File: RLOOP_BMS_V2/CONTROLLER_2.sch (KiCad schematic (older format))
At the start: 38 parts, among them U2 bq76PL536A_HTQFP

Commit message: More WIP
Added connector for 1-Wire sensors if we want to put some sensors on the
heat-sinks. Just need to double check everything with the 3d-models.
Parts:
- U2: symbol bq76PL536A_HTQFP -> bq76PL536A_HTQFP-RESCUE-rLoop_BMS_v2
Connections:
- wire segments 148 -> 149

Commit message: more WIP
So close. Need to finish arranging the sild screen and make sure diodes
get put on in the correct orientation.
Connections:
- net GND_2: now also U2.THRM
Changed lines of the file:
@@
 	6500 4200 6800 4200
 Wire Wire Line
-	6800 4200 6800 4850
+	6800 4100 6800 4850
 Wire Wire Line
 	6500 4300 6800 4300
@@
 Wire Wire Line
 	4250 3400 4100 3400
+Wire Wire Line
+	6500 4100 6800 4100
+Connection ~ 6800 4200
 $EndSCHEMATC

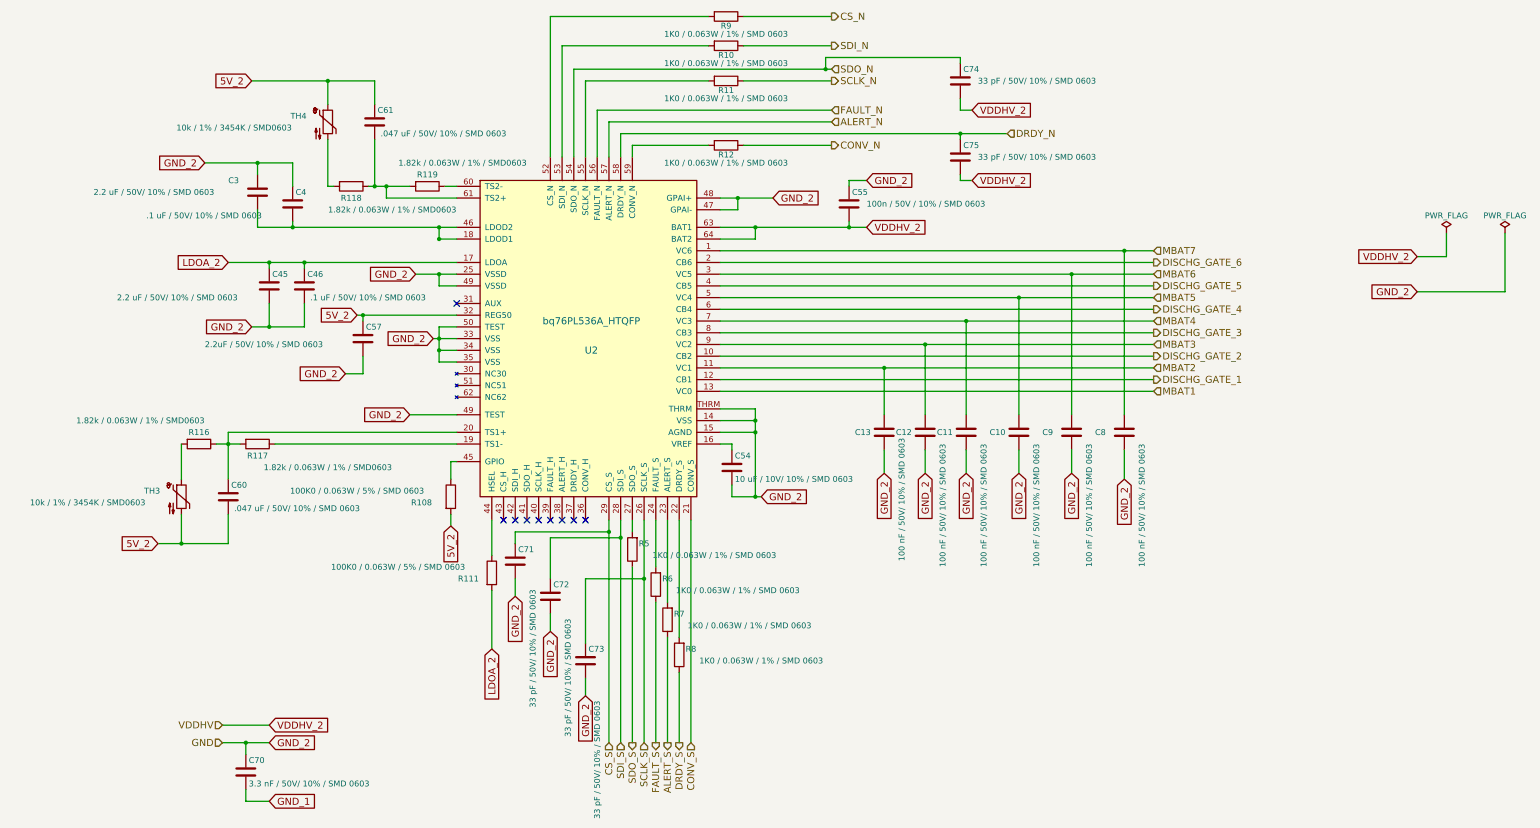
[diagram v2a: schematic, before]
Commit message: Updated page sizes for schematics
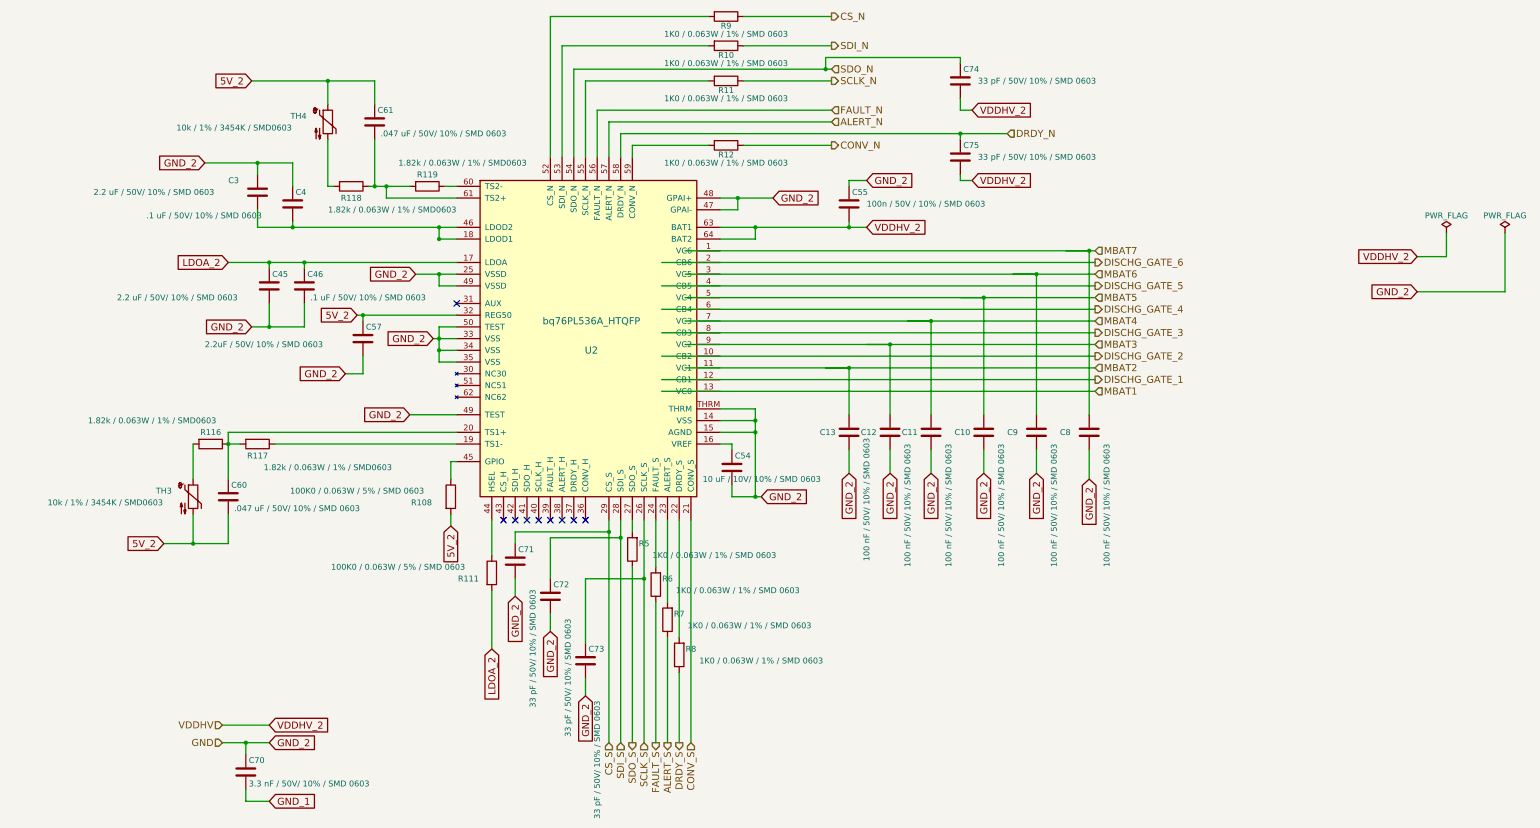
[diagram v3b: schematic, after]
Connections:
- wire segments 150 -> 185
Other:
- moved on the sheet: C10, C11, C12, C13, C8, C9, R116, TH3

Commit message: swapped a few connectors to standardize with the power node and what's readily available
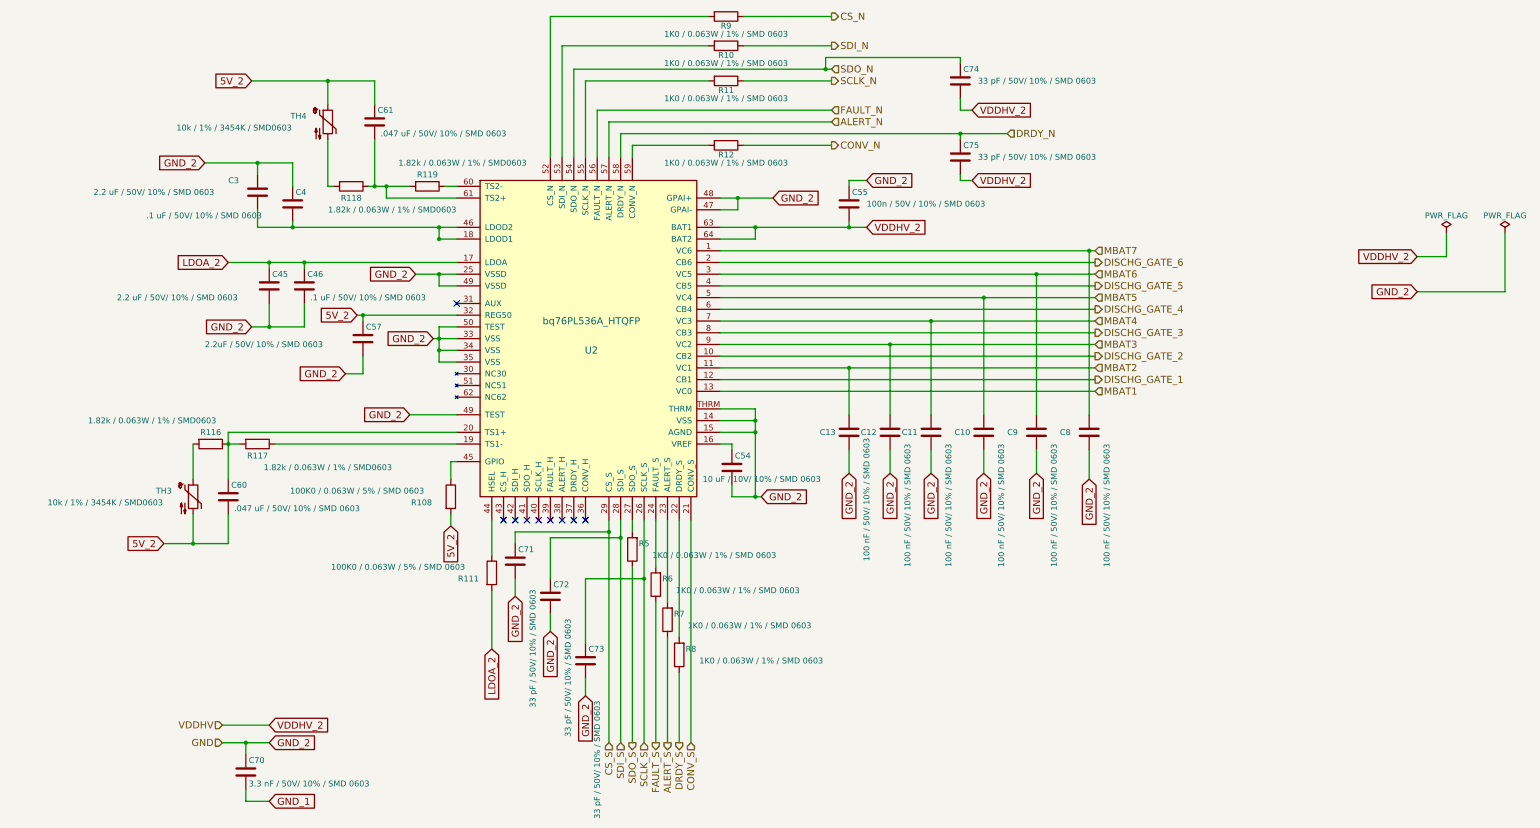
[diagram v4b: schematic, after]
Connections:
- wire segments 185 -> 150
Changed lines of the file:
@@
 	2250 6800 2650 6800
 Wire Wire Line
-	2250 6950 2450 6950
-Wire Wire Line
-	2450 6950 2650 6950
-Wire Wire Line
-	6200 2750 9650 2750
-Wire Wire Line
-	9450 2750 9700 2750
-Wire Wire Line
-	9700 2850 6000 2850
-Wire Wire Line
-	6200 2950 9200 2950
-Wire Wire Line
-	9000 2950 9700 2950
-Wire Wire Line
-	9700 3050 6000 3050
-Wire Wire Line
-	6200 3150 8750 3150
-Wire Wire Line
-	8550 3150 9700 3150
-Wire Wire Line
-	6000 3250 9700 3250
-Wire Wire Line
-	6200 3350 8300 3350
-Wire Wire Line
-	8100 3350 9700 3350
-Wire Wire Line
-	6000 3450 9700 3450
-Wire Wire Line
-	6200 3550 7950 3550
-Wire Wire Line
-	7750 3550 9700 3550
-Wire Wire Line
-	6000 3650 9700 3650
-Wire Wire Line
-	6200 3750 7600 3750
-Wire Wire Line
-	7400 3750 9700 3750
-Wire Wire Line
-	6000 3850 9700 3850
-Wire Wire Line
-	9700 3950 6000 3950
-Wire Wire Line
-	9650 4150 9650 2750
+	2250 6950 2650 6950
+Wire Wire Line
+	6500 2750 9700 2750
+Wire Wire Line
+	6500 2950 9700 2950
+Wire Wire Line
+	6500 3150 9700 3150
+Wire Wire Line
+	6500 3350 9700 3350
+Wire Wire Line
+	6500 3550 9700 3550
+Wire Wire Line
+	6500 3750 9700 3750
+Wire Wire Line
+	9650 2750 9650 4150
 Connection ~ 9650 2750
 Wire Wire Line
-	9200 4150 9200 2950
+	9200 2950 9200 4150
 Connection ~ 9200 2950
 Wire Wire Line
-	8750 4150 8750 3150
+	8750 3150 8750 4150
 Connection ~ 8750 3150
 Wire Wire Line
-	8300 4150 8300 3350
+	8300 3350 8300 4150
 Connection ~ 8300 3350
 Wire Wire Line
-	7950 4150 7950 3550
+	7950 3550 7950 4150
 Connection ~ 7950 3550
 Wire Wire Line
-	7600 4150 7600 3750
+	7600 3750 7600 4150
 Connection ~ 7600 3750
 Wire Wire Line
@@
 	7950 4650 7950 4450
 Wire Wire Line
-	3400 3300 3450 3300
-Wire Wire Line
-	3450 3300 4250 3300
-Wire Wire Line
-	4050 3500 4100 3500
-Wire Wire Line
-	4100 3500 4250 3500
-Wire Wire Line
-	4250 3600 4100 3600
-Wire Wire Line
-	4100 3400 4100 3500
-Wire Wire Line
-	4100 3500 4100 3600
-Wire Wire Line
-	4100 3600 4100 3700
+	3400 3300 4250 3300
+Wire Wire Line
+	4050 3500 4250 3500
+Wire Wire Line
+	4100 3600 4250 3600
+Wire Wire Line
+	4100 3400 4100 3700
 Connection ~ 4100 3500
 Wire Wire Line
@@
 	6500 4200 6800 4200
 Wire Wire Line
-	6800 4100 6800 4200
-Wire Wire Line
-	6800 4200 6800 4300
-Wire Wire Line
-	6800 4300 6800 4850
+	6800 4100 6800 4850
 Wire Wire Line
 	6500 4300 6800 4300
 Connection ~ 6800 4300
 Wire Wire Line
-	3900 2950 4100 2950
-Wire Wire Line
-	4100 2950 4250 2950
+	3900 2950 4250 2950
 Wire Wire Line
 	4250 3050 4100 3050
@@
 Connection ~ 4100 2950
 Wire Wire Line
-	6500 2550 6800 2550
-Wire Wire Line
-	6800 2550 7600 2550
-Wire Wire Line
-	7600 2550 7750 2550
+	6500 2550 7750 2550
 Wire Wire Line
 	6500 2650 6800 2650
@@
 	5250 1950 5250 1200
 Wire Wire Line
-	5250 1200 7400 1200
-Wire Wire Line
-	7400 1200 7450 1200
+	5250 1200 7450 1200
 Wire Wire Line
 	5350 1300 5350 1950
@@
 	5650 1950 5650 1750
 Wire Wire Line
-	5650 1750 8550 1750
-Wire Wire Line
-	8550 1750 8950 1750
+	5650 1750 8950 1750
 Wire Wire Line
 	5550 1950 5550 1650
@@
 	7450 1850 6700 1850
 Wire Wire Line
-	5550 5050 5550 5150
-Wire Wire Line
-	5550 5150 5550 6950
-Wire Wire Line
-	5650 5050 5650 5200
-Wire Wire Line
-	5650 5200 5650 6950
+	5550 5050 5550 6950
+Wire Wire Line
+	5650 5050 5650 6950
 Wire Wire Line
 	5750 5050 5750 5150
@@
 	5750 5450 5750 6950
 Wire Wire Line
-	5850 5050 5850 5550
-Wire Wire Line
-	5850 5550 5850 6950
+	5850 5050 5850 6950
 Wire Wire Line
 	5950 5050 5950 5450
@@
 	5950 5750 5950 6950
 Wire Wire Line
-	2100 2000 2550 2000
-Wire Wire Line
-	2550 2000 2850 2000
+	2100 2000 2850 2000
 Wire Wire Line
 	2550 2000 2550 2100
@@
 Connection ~ 2850 2550
 Wire Wire Line
-	2550 2550 2850 2550
-Wire Wire Line
-	2850 2550 4100 2550
-Wire Wire Line
-	4100 2550 4250 2550
+	2550 2550 4250 2550
 Wire Wire Line
 	2550 2550 2550 2400
@@
 	4100 2650 4250 2650
 Wire Wire Line
-	2500 3400 2650 3400
-Wire Wire Line
-	2650 3400 2950 3400
+	2500 3400 2950 3400
 Wire Wire Line
 	2950 3400 2950 3200
@@
 	2650 2900 2650 2850
 Wire Wire Line
-	2300 2850 2650 2850
-Wire Wire Line
-	2650 2850 2950 2850
-Wire Wire Line
-	2950 2850 4250 2850
+	2300 2850 4250 2850
 Wire Wire Line
 	2950 2900 2950 2850
@@
 	4200 5100 4200 5000
 Wire Wire Line
-	6500 2300 6650 2300
-Wire Wire Line
-	6650 2300 6950 2300
+	6500 2300 6950 2300
 Wire Wire Line
 	6500 2400 6650 2400
@@
 	6600 4400 6600 4450
 Wire Wire Line
-	6600 4850 6800 4850
-Wire Wire Line
-	6800 4850 6850 4850
+	6600 4850 6850 4850
 Wire Wire Line
 	6600 4750 6600 4850
@@
 	3650 2300 3650 2200
 Wire Wire Line
-	3500 2200 3550 2200
-Wire Wire Line
-	3550 2200 3650 2200
-Wire Wire Line
-	3650 2200 3850 2200
+	3500 2200 3850 2200
 Connection ~ 3650 2200
 Wire Wire Line
@@
 	3150 2200 3200 2200
 Wire Wire Line
-	2500 1300 3150 1300
-Wire Wire Line
-	3150 1300 3550 1300
+	2500 1300 3550 1300
 Wire Wire Line
 	3150 1300 3150 1500
@@
 	2000 4700 2000 4400
 Wire Wire Line
-	2300 4400 2300 4400
-Wire Wire Line
 	2300 4400 2400 4400
 Wire Wire Line
 	4250 4300 2300 4300
 Wire Wire Line
-	2300 4300 2300 4400
-Wire Wire Line
-	2300 4400 2300 4700
+	2300 4300 2300 4700
 Connection ~ 2300 4400
 Wire Wire Line
 	2700 4400 4250 4400
 Wire Wire Line
-	1750 5250 2000 5250
-Wire Wire Line
-	2000 5250 2300 5250
+	1750 5250 2300 5250
 Wire Wire Line
 	2000 5250 2000 5000
@@
 	6500 4100 6800 4100
 Connection ~ 6800 4200
+Wire Wire Line
+	6500 2850 9700 2850
+Wire Wire Line
+	6500 3050 9700 3050
+Wire Wire Line
+	6500 3250 9700 3250
+Wire Wire Line
+	6500 3450 9700 3450
+Wire Wire Line
+	6500 3650 9700 3650
+Wire Wire Line
+	6500 3850 9700 3850
+Wire Wire Line
+	9700 3950 6500 3950
 $EndSCHEMATC
